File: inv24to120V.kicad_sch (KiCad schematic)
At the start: 146 parts, among them IC1 NFA50460R4B, J1 0705530003, J10 Screw_Terminal_01x01, J12 Screw_Terminal_01x01, J2 Conn_01x02, J3 Conn_01x02, J7 Screw_Terminal_01x03, Q1 IRFZ44NPBF, Q2 IRFZ44NPBF, Q3 ZXTN2010ZTA, Q4 ZXTN2010ZTA, Q5 ZXTP2012ZTA, Q6 ZXTP2012ZTA, SW1 SW_DIP_x02, U1 ESP32-DEVKITC-32D, U11 ACT45B-220-2P-TL003, U13 FOD817A, U15 FOD817A, U2 LM2576R-5.0, U3 ACS712ELCTR30AT, U4 ACS712ELCTR30AT, U6 ACT45B-220-2P-TL003, U7 ACS712ELCTR30AT, U8 LM2576R-15.0, U9 TJA1040T

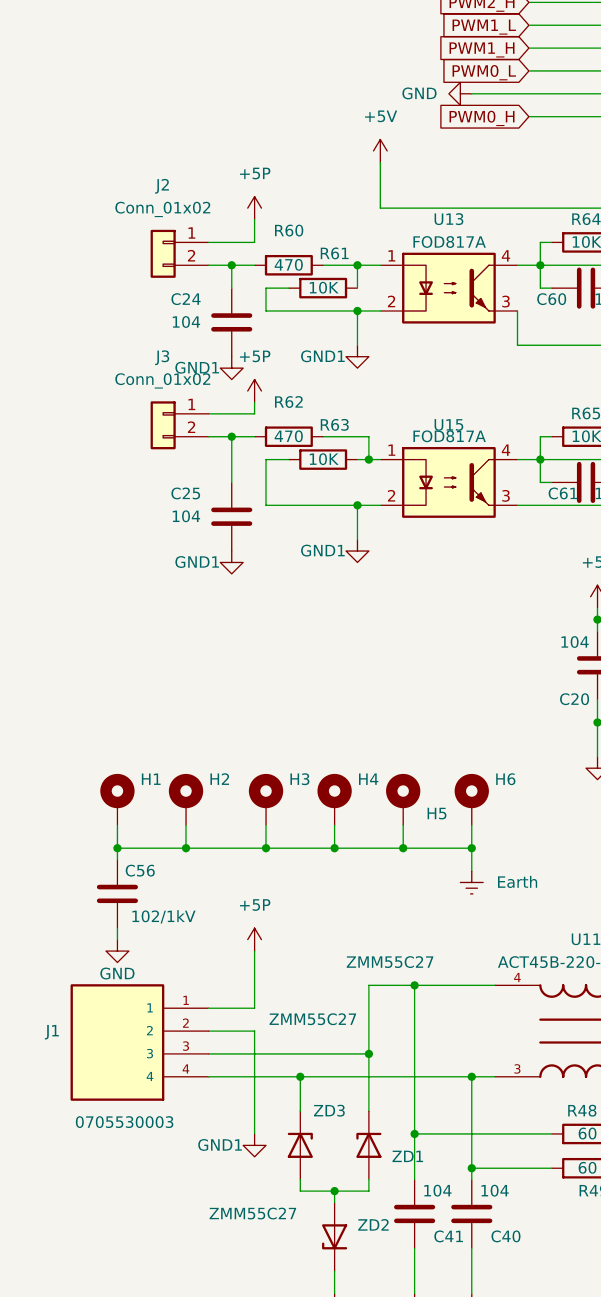
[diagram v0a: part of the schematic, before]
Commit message: fix 35313-0460 0260 dip se 3d model
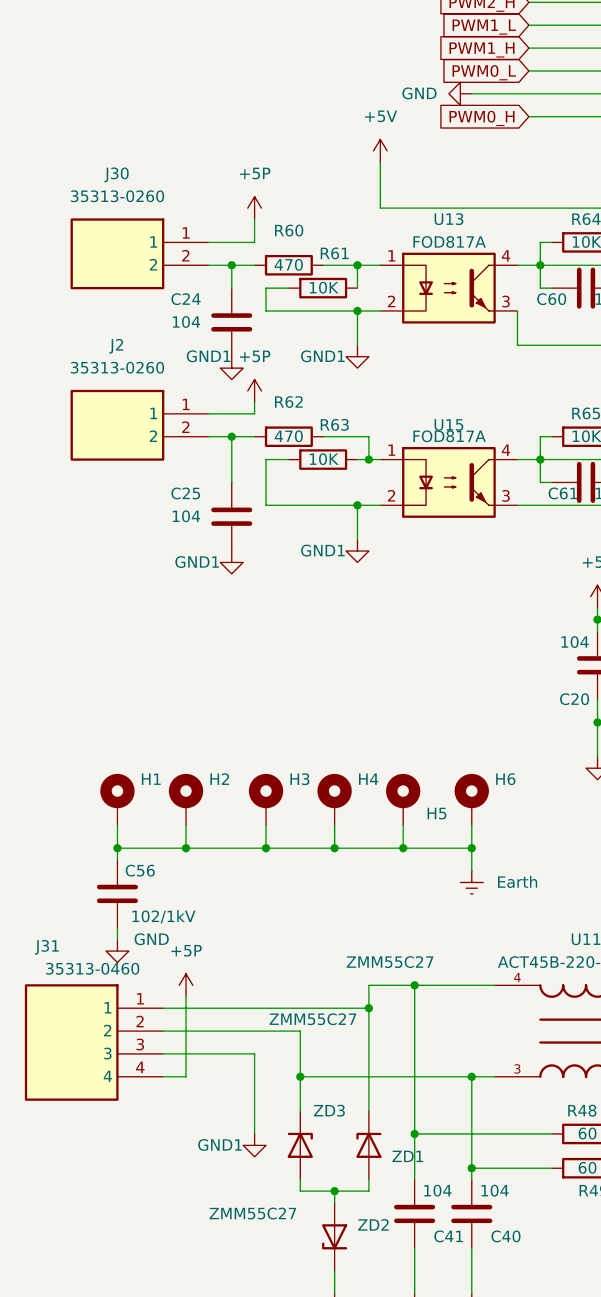
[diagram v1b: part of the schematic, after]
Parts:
- removed J3: Conn_01x02, Connector_Molex:Molex_KK-396_A-41791-0002_1x02_P3.96mm_Vertical, symbol Connector_Generic:Conn_01x02
- added J2: 35313-0260, kilib:SHDR2W107P0X396_1X2_1118X835X1000P, symbol 35313:35313-0260
- J30: renamed from J2; value Conn_01x02 -> 35313-0260; footprint Connector_Molex:Molex_KK-396_A-41791-0002_1x02_P3.96mm_Vertical -> kilib:SHDR2W107P0X396_1X2_1118X835X1000P; symbol Connector_Generic:Conn_01x02 -> 35313:35313-0260; Height (none) -> 10; Manufacturer_Name (none) -> Molex; Manufacturer_Part_Number (none) -> 35313-0260; Mouser Part Number (none) -> 538-35313-0260; Mouser Price/Stock (none) -> https://www.mouser.co.uk/ProductDetail/Molex/35313-0260?qs=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
- J31: renamed from J1; value 0705530003 -> 35313-0460; footprint genCtrlPCB_Lib:MOLEX_0705530039 -> kilib:353130460; symbol 0705530003:0705530003 -> 353130460:35313-0460; Height (none) -> 10; Manufacturer_Name (none) -> Molex; Manufacturer_Part_Number (none) -> 35313-0460; Mouser Part Number (none) -> 538-35313-0460; Mouser Price/Stock (none) -> https://www.mouser.co.uk/ProductDetail/Molex/35313-0460?qs=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
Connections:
- net +5P: now also J31.4, J2.1; no longer J31.1
- net GND1: now also J31.3; no longer J31.2
- net at C40.1, R49.2, U11.3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: now also J31.2; no longer J31.4
- net at C41.1, R48.2, U11.4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: now also J31.1; no longer J31.3
- net at C25.2, R62.2: now also J2.2
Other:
- moved on the sheet: J30, J31
